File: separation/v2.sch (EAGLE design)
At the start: 18 parts, among them Q1 IRLZ24NPBF

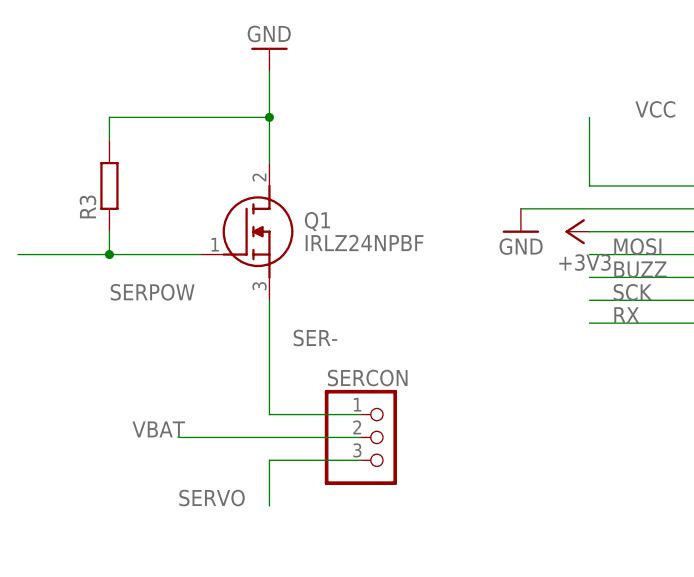
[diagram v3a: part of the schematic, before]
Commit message: fix mosfet connections
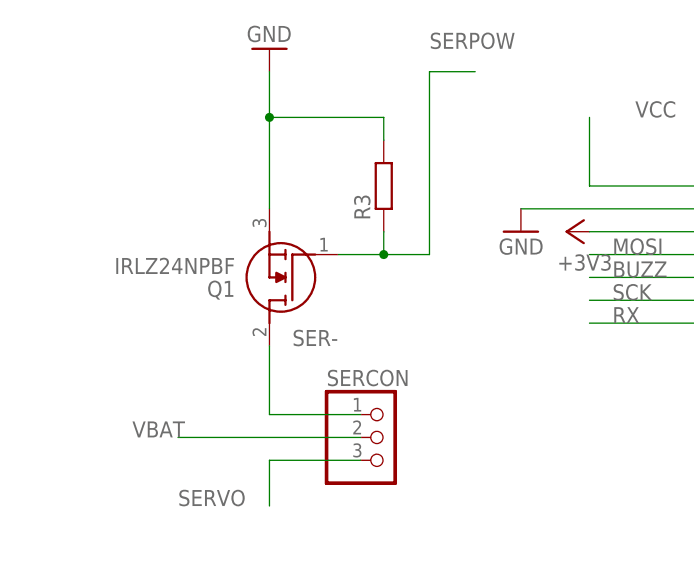
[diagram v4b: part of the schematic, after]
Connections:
- net GND: now also Q1.S; no longer Q1.D
- net SER-: now also Q1.D; no longer Q1.S
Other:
- moved on the sheet: Q1, R3
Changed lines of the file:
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@@
 <attribute name="VALUE" x="63.5" y="-30.48" size="1.778" layer="96" rot="MR0"/>
 </instance>
-<instance part="Q1" gate="G$1" x="-25.4" y="58.42" smashed="yes">
-<attribute name="NAME" x="-13.97" y="62.23" size="1.778" layer="95" align="center-left"/>
-<attribute name="VALUE" x="-13.97" y="59.69" size="1.778" layer="96" align="center-left"/>
+<instance part="Q1" gate="G$1" x="-10.16" y="58.42" smashed="yes" rot="R180">
+<attribute name="NAME" x="-21.59" y="54.61" size="1.778" layer="95" rot="R180" align="center-left"/>
+<attribute name="VALUE" x="-21.59" y="57.15" size="1.778" layer="96" rot="R180" align="center-left"/>
 </instance>
-<instance part="R3" gate="G$1" x="-35.56" y="66.04" smashed="yes" rot="R90">
-<attribute name="NAME" x="-37.0586" y="62.23" size="1.778" layer="95" rot="R90"/>
-<attribute name="VALUE" x="-32.258" y="62.23" size="1.778" layer="96" rot="R90"/>
+<instance part="R3" gate="G$1" x="-5.08" y="66.04" smashed="yes" rot="R90">
+<attribute name="NAME" x="-6.5786" y="62.23" size="1.778" layer="95" rot="R90"/>
+<attribute name="VALUE" x="-1.778" y="62.23" size="1.778" layer="96" rot="R90"/>
 </instance>
 </instances>
@@
 </segment>
 <segment>
-<pinref part="Q1" gate="G$1" pin="D"/>
 <pinref part="GND2" gate="1" pin="GND"/>
-<wire x1="-17.78" y1="68.58" x2="-17.78" y2="73.66" width="0.1524" layer="91"/>
+<pinref part="Q1" gate="G$1" pin="S"/>
+<wire x1="-17.78" y1="63.5" x2="-17.78" y2="73.66" width="0.1524" layer="91"/>
 <pinref part="R3" gate="G$1" pin="2"/>
 <wire x1="-17.78" y1="73.66" x2="-17.78" y2="78.74" width="0.1524" layer="91"/>
-<wire x1="-35.56" y1="71.12" x2="-35.56" y2="73.66" width="0.1524" layer="91"/>
-<wire x1="-35.56" y1="73.66" x2="-17.78" y2="73.66" width="0.1524" layer="91"/>
+<wire x1="-5.08" y1="71.12" x2="-5.08" y2="73.66" width="0.1524" layer="91"/>
+<wire x1="-5.08" y1="73.66" x2="-17.78" y2="73.66" width="0.1524" layer="91"/>
 <junction x="-17.78" y="73.66"/>
 </segment>
@@
 <pinref part="SERCON" gate="A" pin="1"/>
 <wire x1="-7.62" y1="40.64" x2="-17.78" y2="40.64" width="0.1524" layer="91"/>
-<pinref part="Q1" gate="G$1" pin="S"/>
-<wire x1="-17.78" y1="40.64" x2="-17.78" y2="53.34" width="0.1524" layer="91"/>
 <label x="-15.24" y="48.26" size="1.778" layer="95"/>
+<pinref part="Q1" gate="G$1" pin="D"/>
+<wire x1="-17.78" y1="48.26" x2="-17.78" y2="40.64" width="0.1524" layer="91"/>
 </segment>
 </net>
 <net name="SERPOW" class="0">
-<segment>
-<pinref part="Q1" gate="G$1" pin="G"/>
-<wire x1="-25.4" y1="58.42" x2="-35.56" y2="58.42" width="0.1524" layer="91"/>
-<label x="-35.56" y="53.34" size="1.778" layer="95"/>
-<pinref part="R3" gate="G$1" pin="1"/>
-<wire x1="-35.56" y1="60.96" x2="-35.56" y2="58.42" width="0.1524" layer="91"/>
-<wire x1="-35.56" y1="58.42" x2="-45.72" y2="58.42" width="0.1524" layer="91"/>
-<junction x="-35.56" y="58.42"/>
-</segment>
 <segment>
 <label x="45.72" y="58.42" size="1.778" layer="95"/>
@@
 <wire x1="58.42" y1="58.42" x2="45.72" y2="58.42" width="0.1524" layer="91"/>
 </segment>
-</net>
+<segment>
+<pinref part="Q1" gate="G$1" pin="G"/>
+<wire x1="-10.16" y1="58.42" x2="-5.08" y2="58.42" width="0.1524" layer="91"/>
+<pinref part="R3" gate="G$1" pin="1"/>
+<wire x1="-5.08" y1="58.42" x2="-5.08" y2="60.96" width="0.1524" layer="91"/>
+<wire x1="-5.08" y1="58.42" x2="0" y2="58.42" width="0.1524" layer="91"/>
+<junction x="-5.08" y="58.42"/>
+<wire x1="0" y1="58.42" x2="0" y2="78.74" width="0.1524" layer="91"/>
+<wire x1="0" y1="78.74" x2="5.08" y2="78.74" width="0.1524" layer="91"/>
+<label x="0" y="81.28" size="1.778" layer="95"/>
+</segment>
+</net>

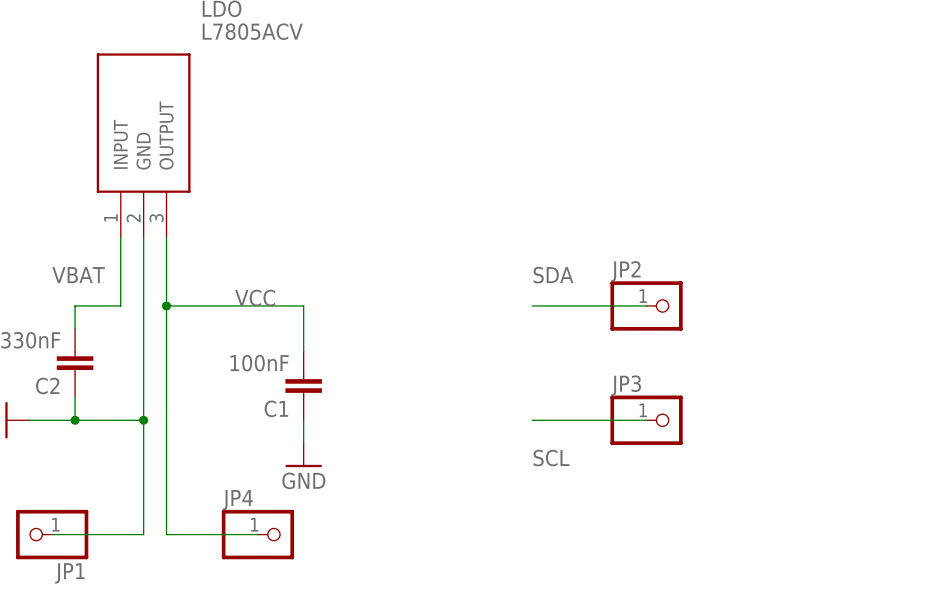
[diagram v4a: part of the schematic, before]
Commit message: add diode on regulator output
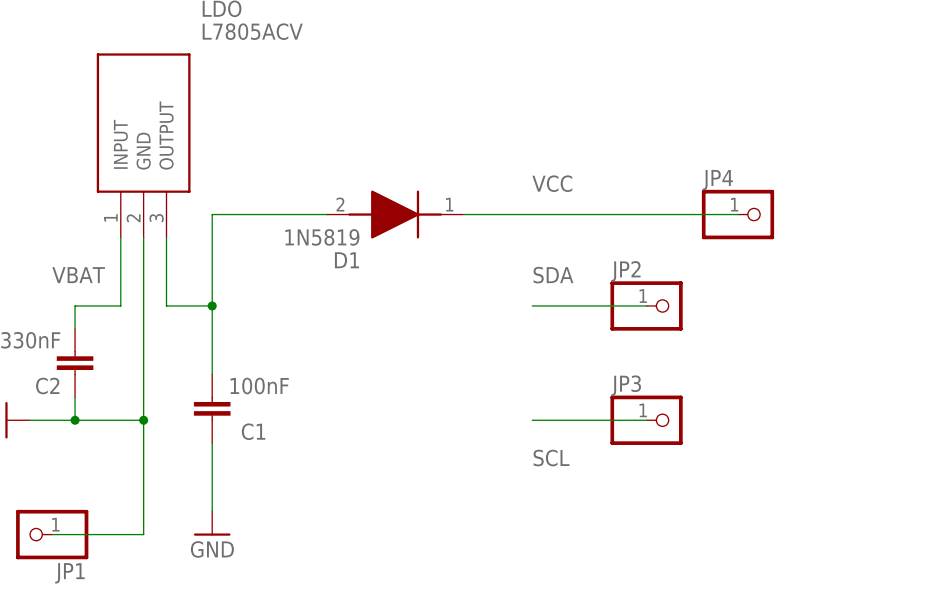
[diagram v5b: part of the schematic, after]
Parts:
- added D1: 1N5819, SamacSys_Parts:1N5819
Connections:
- new net VOUT: C1.2, D1.A, LDO.OUTPUT
- net VCC: now also D1.K; no longer C1.2, LDO.OUTPUT
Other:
- moved on the sheet: C1, JP4
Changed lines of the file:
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@@
 <part name="Q1" library="SamacSys_Parts" deviceset="IRLZ24NPBF" device=""/>
 <part name="R3" library="rcl" library_urn="urn:adsk.eagle:library:334" deviceset="R-EU_" device="0204/2V" package3d_urn="urn:adsk.eagle:package:23495/1"/>
+<part name="D1" library="SamacSys_Parts" deviceset="1N5819" device=""/>
 </parts>
 <sheets>
@@
 <attribute name="VALUE" x="36.83" y="-30.48" size="1.778" layer="96" rot="R180"/>
 </instance>
-<instance part="JP4" gate="G$1" x="58.42" y="-35.56" smashed="yes">
-<attribute name="NAME" x="52.07" y="-32.385" size="1.778" layer="95"/>
-<attribute name="VALUE" x="52.07" y="-40.64" size="1.778" layer="96"/>
-</instance>
-<instance part="C1" gate="G$1" x="60.96" y="-20.32" smashed="yes" rot="R180">
-<attribute name="NAME" x="59.436" y="-20.701" size="1.778" layer="95" rot="R180"/>
-<attribute name="VALUE" x="59.436" y="-15.621" size="1.778" layer="96" rot="R180"/>
+<instance part="JP4" gate="G$1" x="111.76" y="0" smashed="yes">
+<attribute name="NAME" x="105.41" y="3.175" size="1.778" layer="95"/>
+<attribute name="VALUE" x="105.41" y="-5.08" size="1.778" layer="96"/>
+</instance>
+<instance part="C1" gate="G$1" x="50.8" y="-22.86" smashed="yes" rot="R180">
+<attribute name="NAME" x="56.896" y="-23.241" size="1.778" layer="95" rot="R180"/>
+<attribute name="VALUE" x="59.436" y="-18.161" size="1.778" layer="96" rot="R180"/>
 </instance>
 <instance part="C2" gate="G$1" x="35.56" y="-17.78" smashed="yes" rot="R180">
@@
 <attribute name="VALUE" x="34.036" y="-13.081" size="1.778" layer="96" rot="R180"/>
 </instance>
-<instance part="GND7" gate="1" x="60.96" y="-27.94" smashed="yes" rot="MR0">
-<attribute name="VALUE" x="63.5" y="-30.48" size="1.778" layer="96" rot="MR0"/>
+<instance part="GND7" gate="1" x="50.8" y="-35.56" smashed="yes" rot="MR0">
+<attribute name="VALUE" x="53.34" y="-38.1" size="1.778" layer="96" rot="MR0"/>
 </instance>
 <instance part="Q1" gate="G$1" x="-10.16" y="58.42" smashed="yes" rot="R180">
@@
 <attribute name="NAME" x="-6.5786" y="62.23" size="1.778" layer="95" rot="R90"/>
 <attribute name="VALUE" x="-1.778" y="62.23" size="1.778" layer="96" rot="R90"/>
+</instance>
+<instance part="D1" gate="G$1" x="78.74" y="0" smashed="yes" rot="R180">
+<attribute name="NAME" x="67.31" y="-5.08" size="1.778" layer="95" rot="R180" align="center-left"/>
+<attribute name="VALUE" x="67.31" y="-2.54" size="1.778" layer="96" rot="R180" align="center-left"/>
 </instance>
 </instances>
@@
 <segment>
 <pinref part="GND7" gate="1" pin="GND"/>
-<wire x1="60.96" y1="-25.4" x2="60.96" y2="-22.86" width="0.1524" layer="91"/>
+<wire x1="50.8" y1="-33.02" x2="50.8" y2="-25.4" width="0.1524" layer="91"/>
 <pinref part="C1" gate="G$1" pin="1"/>
 </segment>
@@
 </segment>
 <segment>
-<pinref part="LDO" gate="G$1" pin="OUTPUT"/>
-<wire x1="45.72" y1="-2.54" x2="45.72" y2="-10.16" width="0.1524" layer="91"/>
-<label x="53.34" y="-10.16" size="1.778" layer="95"/>
-<junction x="45.72" y="-10.16"/>
-<wire x1="45.72" y1="-10.16" x2="45.72" y2="-35.56" width="0.1524" layer="91"/>
+<pinref part="D1" gate="G$1" pin="K"/>
+<wire x1="78.74" y1="0" x2="109.22" y2="0" width="0.1524" layer="91"/>
 <pinref part="JP4" gate="G$1" pin="1"/>
-<wire x1="45.72" y1="-35.56" x2="55.88" y2="-35.56" width="0.1524" layer="91"/>
-<wire x1="45.72" y1="-10.16" x2="60.96" y2="-10.16" width="0.1524" layer="91"/>
-<pinref part="C1" gate="G$1" pin="2"/>
-<wire x1="60.96" y1="-10.16" x2="60.96" y2="-15.24" width="0.1524" layer="91"/>
+<label x="86.36" y="2.54" size="1.778" layer="95"/>
 </segment>
 </net>
@@
 </segment>
 </net>
+<net name="VOUT" class="1">
+<segment>
+<pinref part="LDO" gate="G$1" pin="OUTPUT"/>
+<wire x1="45.72" y1="-2.54" x2="45.72" y2="-10.16" width="0.1524" layer="91"/>
+<wire x1="45.72" y1="-10.16" x2="50.8" y2="-10.16" width="0.1524" layer="91"/>
+<pinref part="C1" gate="G$1" pin="2"/>
+<wire x1="50.8" y1="-10.16" x2="50.8" y2="-17.78" width="0.1524" layer="91"/>
+<wire x1="50.8" y1="-10.16" x2="50.8" y2="0" width="0.1524" layer="91"/>
+<junction x="50.8" y="-10.16"/>
+<pinref part="D1" gate="G$1" pin="A"/>
+<wire x1="50.8" y1="0" x2="63.5" y2="0" width="0.1524" layer="91"/>
+</segment>
+</net>

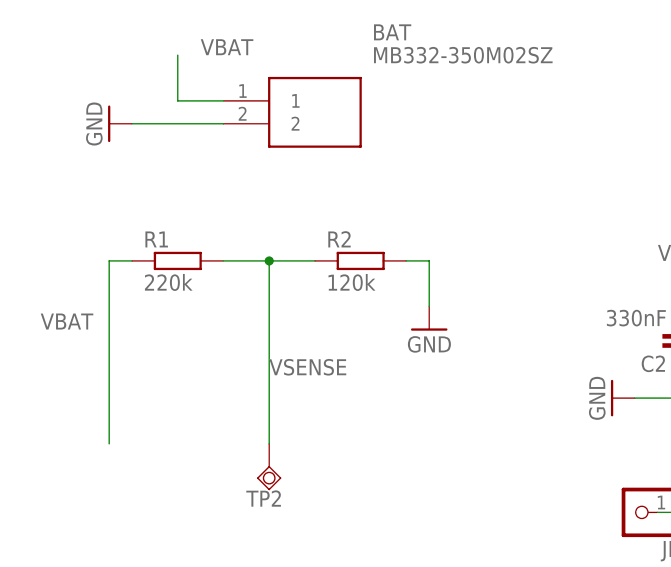
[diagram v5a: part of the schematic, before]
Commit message: fix voltage divider vals
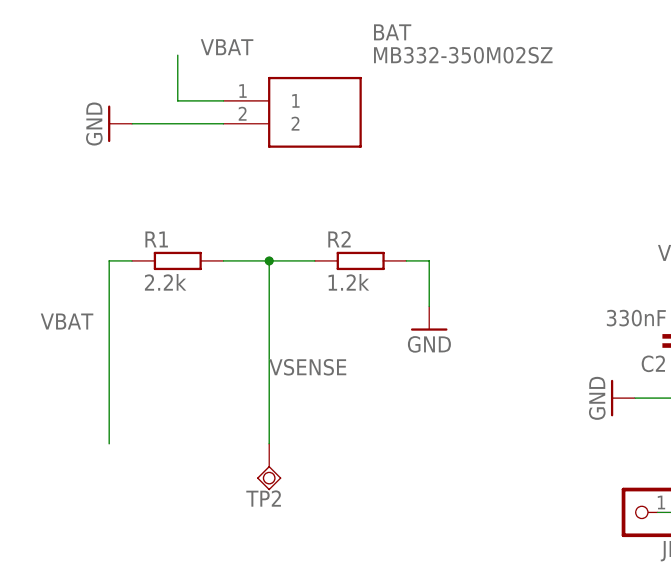
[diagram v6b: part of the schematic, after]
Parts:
- R1: value 220k -> 2.2k
- R2: value 120k -> 1.2k
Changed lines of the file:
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@@
 <part name="GND4" library="supply1" library_urn="urn:adsk.eagle:library:371" deviceset="GND" device=""/>
 <part name="GND5" library="supply1" library_urn="urn:adsk.eagle:library:371" deviceset="GND" device=""/>
-<part name="R1" library="rcl" library_urn="urn:adsk.eagle:library:334" deviceset="R-EU_" device="0204/2V" package3d_urn="urn:adsk.eagle:package:23495/1" value="220k"/>
-<part name="R2" library="rcl" library_urn="urn:adsk.eagle:library:334" deviceset="R-EU_" device="0204/2V" package3d_urn="urn:adsk.eagle:package:23495/1" value="120k"/>
+<part name="R1" library="rcl" library_urn="urn:adsk.eagle:library:334" deviceset="R-EU_" device="0204/2V" package3d_urn="urn:adsk.eagle:package:23495/1" value="2.2k"/>
+<part name="R2" library="rcl" library_urn="urn:adsk.eagle:library:334" deviceset="R-EU_" device="0204/2V" package3d_urn="urn:adsk.eagle:package:23495/1" value="1.2k"/>
 <part name="GND6" library="supply1" library_urn="urn:adsk.eagle:library:371" deviceset="GND" device=""/>
 <part name="TP2" library="testpad" library_urn="urn:adsk.eagle:library:385" deviceset="TPSQ" device="B2,54" package3d_urn="urn:adsk.eagle:package:27948/1"/>
